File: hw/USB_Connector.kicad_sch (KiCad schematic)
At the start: 6 parts, among them J1 USB_C_Receptacle_USB2.0_16P, U4 SRV05-4

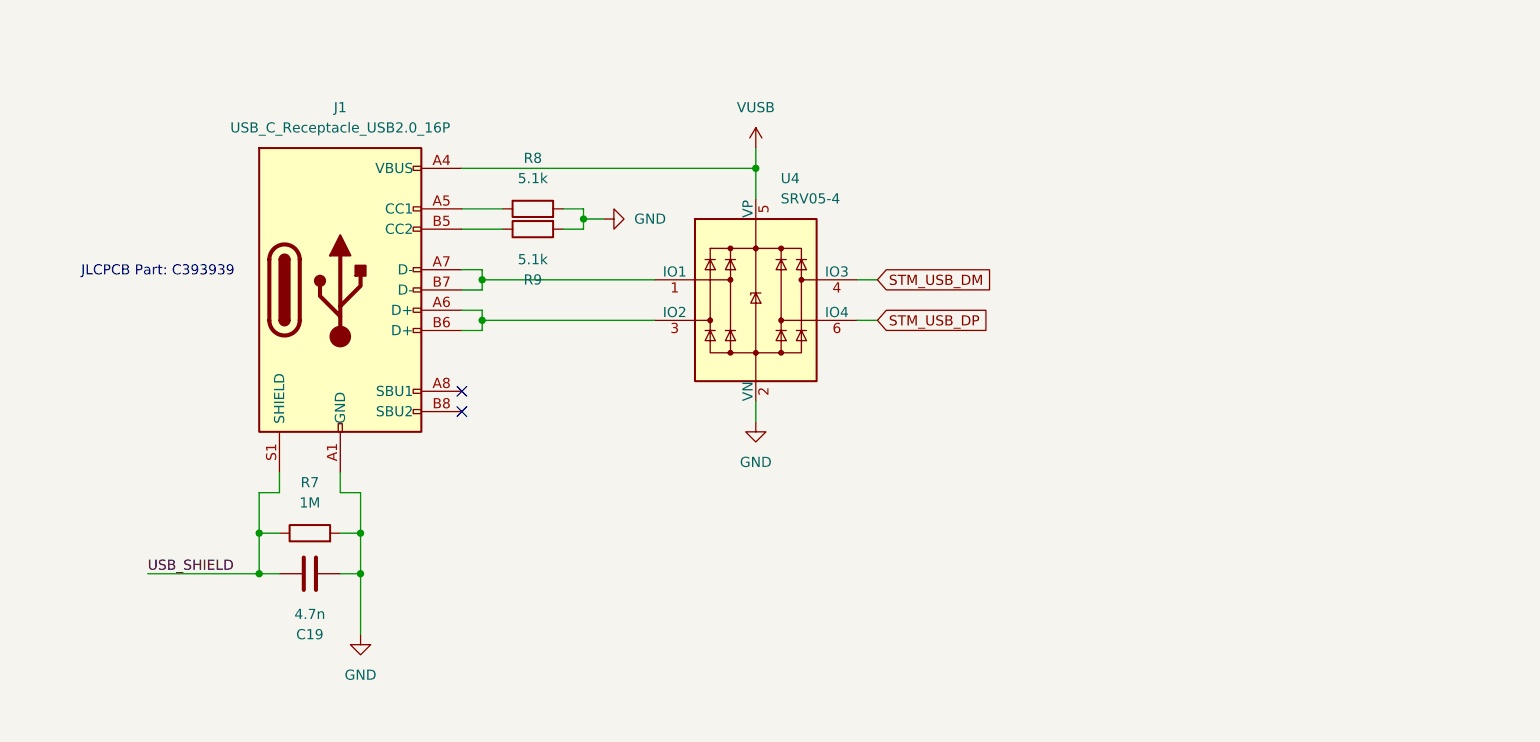
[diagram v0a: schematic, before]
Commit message: updated hardware issues for PBC revision 2
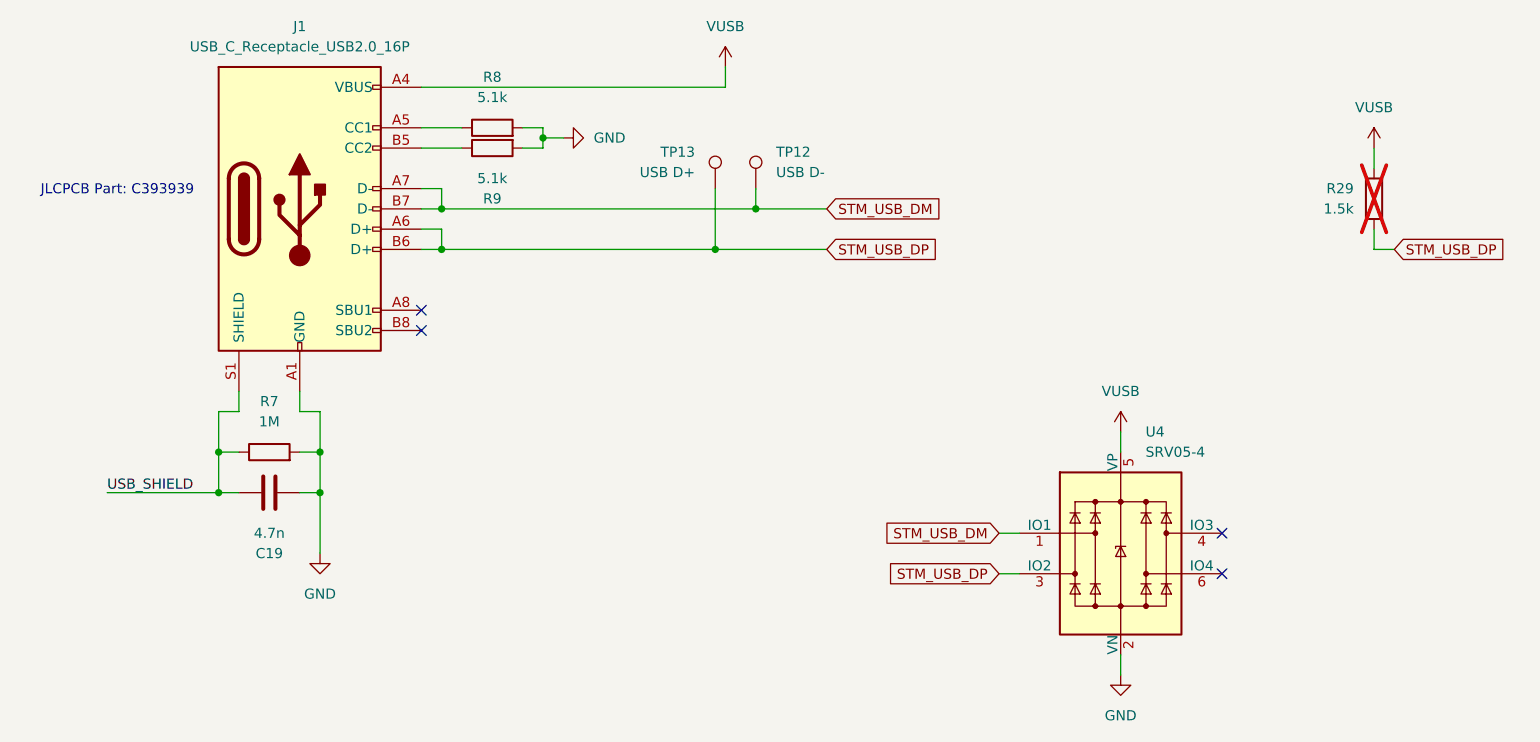
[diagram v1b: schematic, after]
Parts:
- added R29: 1.5k, Resistor_SMD:R_0603_1608Metric, symbol Device:R
- added TP12: USB D-, TestPoint:TestPoint_Pad_D2.0mm, symbol Connector:TestPoint
- added TP13: USB D+, TestPoint:TestPoint_Pad_D2.0mm, symbol Connector:TestPoint
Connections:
- net STM_USB_DM: now also J1.A7 (D-), J1.B7 (D-), U4.1 (IO1), TP12.1; no longer U4.4 (IO3)
- net STM_USB_DP: now also J1.A6 (D+), J1.B6 (D+), U4.3 (IO2), R29.1, TP13.1; no longer U4.6 (IO4)
- net VUSB: now also R29.2
- no-connect marks 2 -> 4
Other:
- moved on the sheet: C19, J1, R7, R8, R9, U4
